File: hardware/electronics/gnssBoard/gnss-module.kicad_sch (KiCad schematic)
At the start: 41 parts, among them Q1 BSS138PS,115, Q2 BSS138PS,115, Q3 VAL, U2 ZED-F9P, U3 OPA344

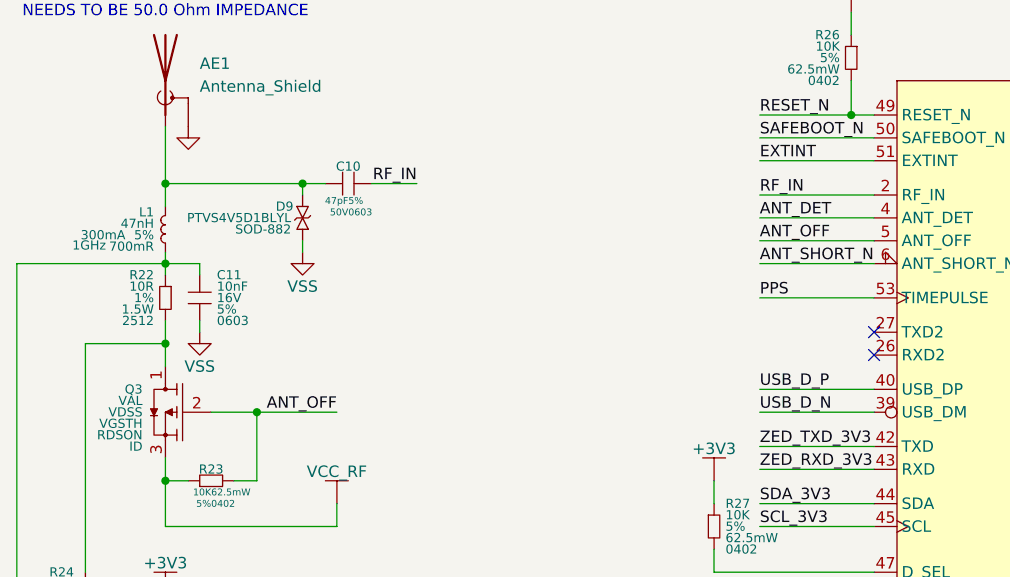
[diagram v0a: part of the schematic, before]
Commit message: applied netclasses
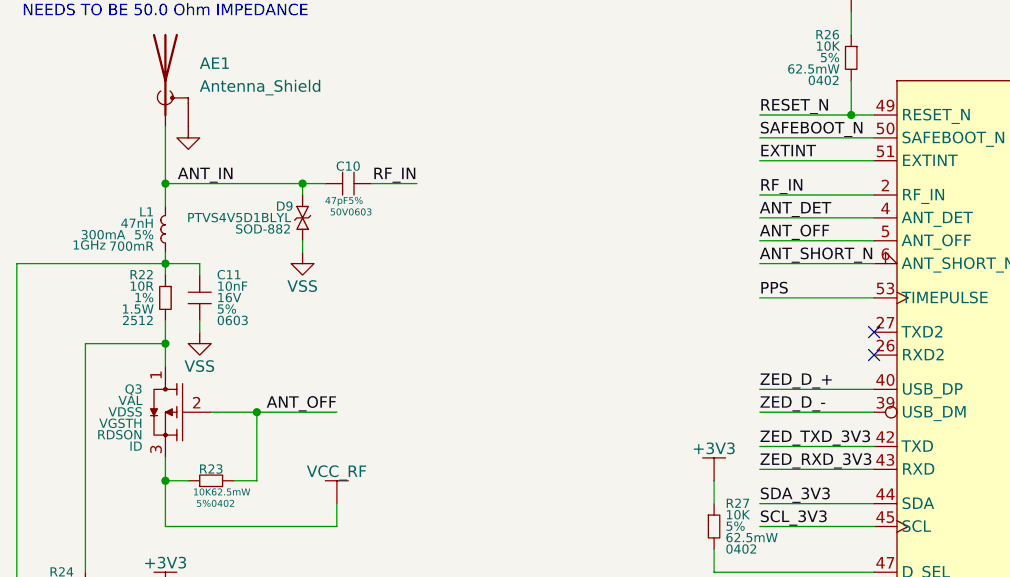
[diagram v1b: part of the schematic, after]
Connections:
- net ANT_IN: now reaches AE1.1 (A), C10.1, D9.2, L1.1
- net USB_D_N renamed ZED_D_-
- net USB_D_P renamed ZED_D_+
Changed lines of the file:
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@@
 		)
 	)
-	(label "USB_D_P"
+	(label "ZED_D_+"
 		(at 114.3 106.68 0)
 		(fields_autoplaced yes)
@@
 		)
 	)
-	(label "USB_D_N"
+	(label "ZED_D_-"
 		(at 114.3 109.22 0)
 		(fields_autoplaced yes)
@@
 		)
 	)
+	(label "ANT_IN"
+		(at 55.88 83.82 180)
+		(fields_autoplaced yes)
+		(effects
+			(font
+				(size 1.27 1.27)
+			)
+			(justify right bottom)
+		)
+	)

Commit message: work on schematic
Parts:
- AE1: value Antenna_Shield -> CONMHF1-SMD-T; footprint (none) -> lib_fp:CONMHF1; DKPN (none) -> 343-CONMHF1-SMD-TCT-ND; MPN (none) -> CONMHF1-SMD-T; Manufacturer (none) -> TE Connectivity Linx
- BT1: footprint (none) -> lib_fp:MS621FE-FL11E; CELL CELL -> Coin, 6.8mm; DKPN (none) -> 728-1057-ND; MPN (none) -> MS621FE-FL11E; Manufacturer (none) -> Seiko Instruments
- C10, C11, C5, C6, C7, C8, C9: footprint (none) -> DS-Capacitors-SMD:MLCC0603
- D7: footprint (none) -> lib_fp:LTST-0603
- D8: footprint (none) -> lib_fp:SOD123
- D9: footprint (none) -> lib_fp:SOD882
- L1: footprint (none) -> lib_fp:L_0402
- Q1, Q2: footprint (none) -> lib_fp:SOT23-6P65_210X200x110L30X25N
- Q3: value VAL -> DMG1013TQ-7; footprint (none) -> lib_fp:SOT23-3P50_160X160X75L22X22N; DKPN (none) -> 31-DMG1013TQ-7CT-ND; MPN (none) -> DMG1013TQ-7; Manufacturer (none) -> Diodes Incorporated
- R12, R13, R14, R15, R16, R17, R18, R19, R20, R21, R23, R24, R25, R26, R27: footprint (none) -> lib_fp:CRCW0402
- R22: footprint (none) -> lib_fp:CRCW2512-HP
- TP11, TP12, TP13, TP14, TP15, TP16: footprint (none) -> lib_fp:TP_1mm; DKPN (none) -> N/A; MPN (none) -> N/A; Manufacturer (none) -> N/A; now left out of the parts list
- U2: footprint DSE-RF-Receivers:ZED-F9P-04B_UBL -> lib_fp:ZED-F9P-04B_UBL
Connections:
- net ANT_OFF: now also Q3.1; no longer Q3.2
- net ANT_SHORT_N: now also U3.4 (-); no longer U3.3 (V-)
- net VCC_RF: now also Q3.2; no longer Q3.3
- net VSS: now also U3.2 (V-); no longer U3.3 (V-)
- net at R22.2, R24.1: now also Q3.3; no longer Q3.1
- net at R24.2, R25.1: now also U3.3 (+); no longer U3.4 (+)

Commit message: worked on GNSS board
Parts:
- removed Q1, Q2: BSS138PS,115, lib_fp:SOT23-6P65_210X200x110L30X25N, symbol lib_sch:Duel-NMOS
- added C5: 100nF, lib_fp:MLCC0603, symbol lib_sch:C
- added Q1, Q2, Q3, Q4: DMN2992UFB4Q-7B, lib_fp:XDFN3P35_100X60X40L15X25N, symbol DS-Transistors:NMOS_GSD
- added R21, R22: 27R, lib_fp:CRCW0402, symbol lib_sch:R_horizontal
- AE1: symbol Device:Antenna_Shield -> lib_sch:Antenna_Shield
- BT1: symbol DS-Batteries:Battery -> lib_sch:Battery
- C10: renamed from C11; footprint DS-Capacitors-SMD:MLCC0603 -> lib_fp:MLCC0603; symbol DS-Passives:C -> lib_sch:C
- C3: renamed from C5; footprint DS-Capacitors-SMD:MLCC0603 -> lib_fp:MLCC0603; symbol DS-Passives:C -> lib_sch:C
- C4: renamed from C6; footprint DS-Capacitors-SMD:MLCC0603 -> lib_fp:MLCC0603; symbol DS-Passives:C -> lib_sch:C
- C6: renamed from C7; footprint DS-Capacitors-SMD:MLCC0603 -> lib_fp:MLCC0603; symbol DS-Passives:C -> lib_sch:C
- C7: renamed from C8; footprint DS-Capacitors-SMD:MLCC0603 -> lib_fp:MLCC0603; symbol DS-Passives:C -> lib_sch:C
- C8: renamed from C9; footprint DS-Capacitors-SMD:MLCC0603 -> lib_fp:MLCC0603; symbol DS-Passives:C -> lib_sch:C
- C9: renamed from C10; footprint DS-Capacitors-SMD:MLCC0603 -> lib_fp:MLCC0603; symbol DS-Passives:C_horizontal -> lib_sch:C_horizontal
- D4: renamed from D7; symbol DS-LEDs:LED -> lib_sch:LED
- D5: renamed from D8; symbol DS-Passives:D_Schottky -> lib_sch:D_Schottky
- D6: renamed from D9; symbol DS-Passives:D_TVS -> lib_sch:D_TVS
- JP4: footprint (none) -> lib_fp:Jumper_2_Bridged; symbol DS-Jumpers:Jumper_2_Bridged -> lib_sch:Jumper_2_Bridged
- L1: symbol DS-Passives:L -> lib_sch:L
- Q5: renamed from Q3; symbol DS-Transistors:PMOS_DGS -> lib_sch:PMOS_DGS
- R10: renamed from R16; symbol DS-Passives:R -> lib_sch:R
- R11: renamed from R17; symbol DS-Passives:R -> lib_sch:R
- R12: renamed from R18; symbol DS-Passives:R -> lib_sch:R
- R13: renamed from R19; symbol DS-Passives:R -> lib_sch:R
- R14: renamed from R20; symbol DS-Passives:R -> lib_sch:R
- R15: renamed from R21; symbol DS-Passives:R -> lib_sch:R
- R16: renamed from R22; footprint lib_fp:CRCW2512-HP -> lib_fp:CRCW0603; symbol DS-Passives:R -> lib_sch:R; DKPN 541-10.0RCT-ND -> 541-10.0HCT-ND; MPN CRCW251210R0FKEGHP -> CRCW060310R0FKEA; Package 2512 -> 0603; Power Rating 1.5W -> 100mW
- R17: renamed from R23; symbol DS-Passives:R_horizontal -> lib_sch:R_horizontal
- R18: renamed from R24; symbol DS-Passives:R -> lib_sch:R
- R19: renamed from R25; symbol DS-Passives:R -> lib_sch:R
- R20: renamed from R26; symbol DS-Passives:R -> lib_sch:R
- R23: renamed from R27; symbol DS-Passives:R -> lib_sch:R
- R6: renamed from R12; symbol DS-Passives:R -> lib_sch:R
- R7: renamed from R13; symbol DS-Passives:R -> lib_sch:R
- R8: renamed from R14; symbol DS-Passives:R -> lib_sch:R
- R9: renamed from R15; symbol DS-Passives:R -> lib_sch:R
- TP11, TP12, TP13, TP14, TP15, TP16: symbol DS-Testpoints:Testpoint -> lib_sch:Testpoint
- U2: symbol DS-RF-Receivers:ZED-F9P-04B -> lib_sch:ZED-F9P-04B
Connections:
- net VBUS is gone; now on net +3V3: C6.1, C7.1, U2.38 (V_USB)
- net +1V8: now also Q1.1, Q2.1, Q3.1, Q4.1
- net +3V3: now also C5.1
- net PPS: now also R14.1; no longer D4.1
- net SCL_3V3: now also Q1.3
- net SDA_1V8: now also Q2.2; no longer R8.2
- net SDA_3V3: now also Q2.3
- net VSS: now also C5.2
- net ZED_RXD_1V8: now also Q3.2; no longer R13.2
- net ZED_RXD_3V3: now also Q3.3
- net ZED_TXD_3V3: now also Q4.3
- net at D4.2: now also JP4.2; no longer R14.1
- net at R14.2: now also D4.1; no longer JP4.2
- net ZED_D_+ renamed ZED_D+
- net ZED_D+: now also R21.2
- net ZED_D_- renamed ZED_D-
- net ZED_D-: now also R22.2
- new net HOST_D+: R21.1
- new net HOST_D-: R22.1
- new net SCL_1V8: Q1.2, R8.2
- new net ZED_TXD_1V8: Q4.2, R13.2
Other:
- moved on the sheet: C3, C4, D4, JP4, R14, R23

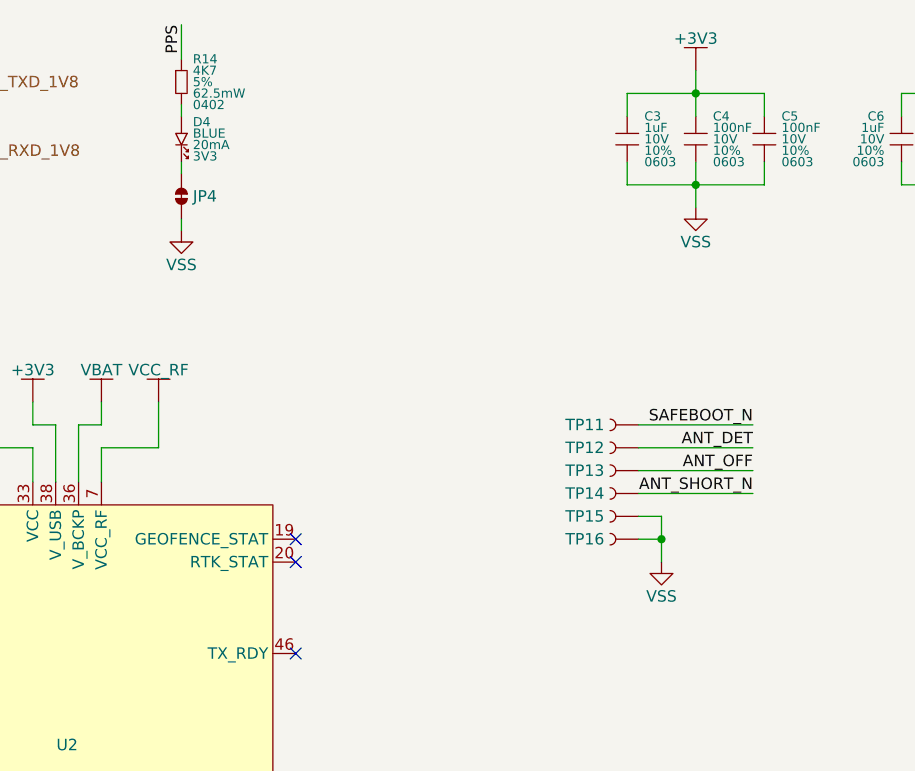
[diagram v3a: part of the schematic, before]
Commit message: Got rid of test points due to space constraints
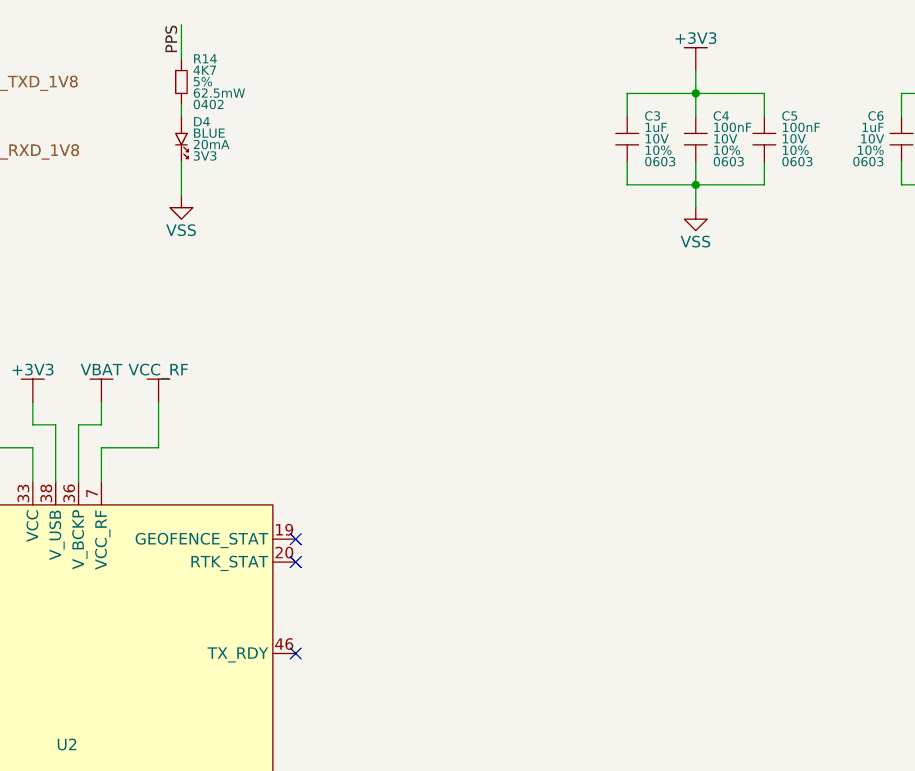
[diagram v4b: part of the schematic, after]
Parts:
- removed JP4: ~, lib_fp:Jumper_2_Bridged, symbol lib_sch:Jumper_2_Bridged
- removed TP11, TP12, TP13, TP14, TP15, TP16: ~, lib_fp:TP_1mm, symbol lib_sch:Testpoint
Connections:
- net VSS: now also D4.2

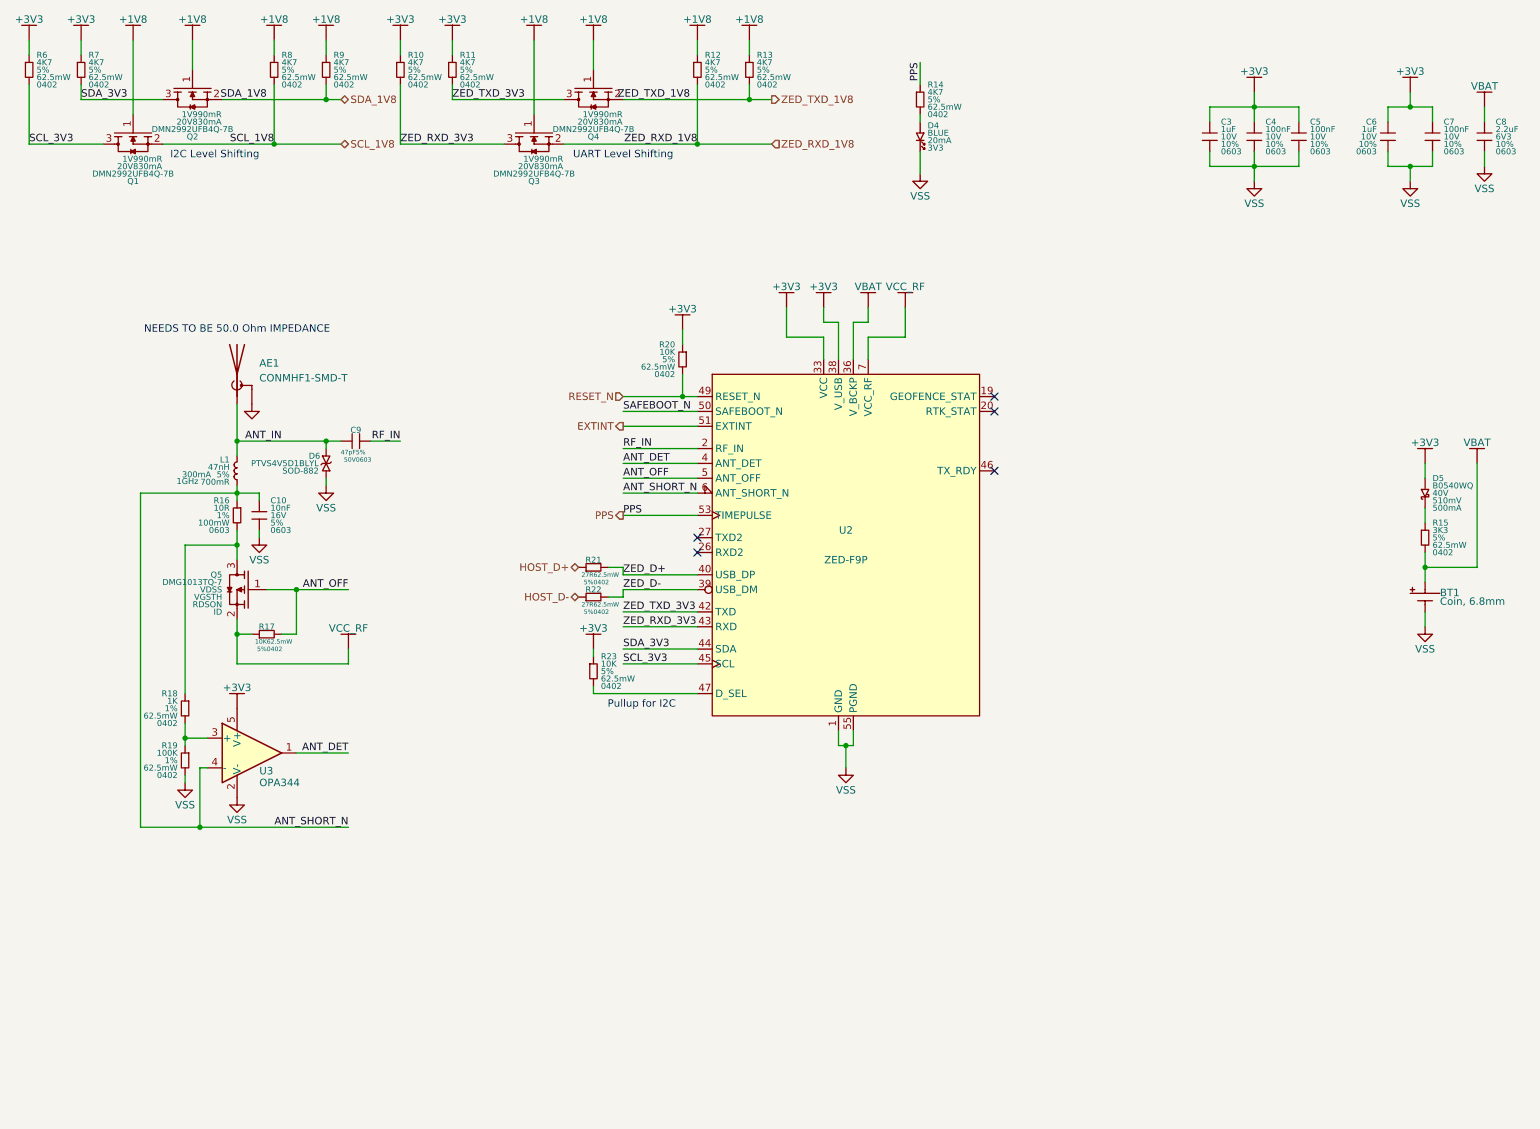
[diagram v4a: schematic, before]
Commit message: replaced MOSFETS with TI multi-channel level shifter
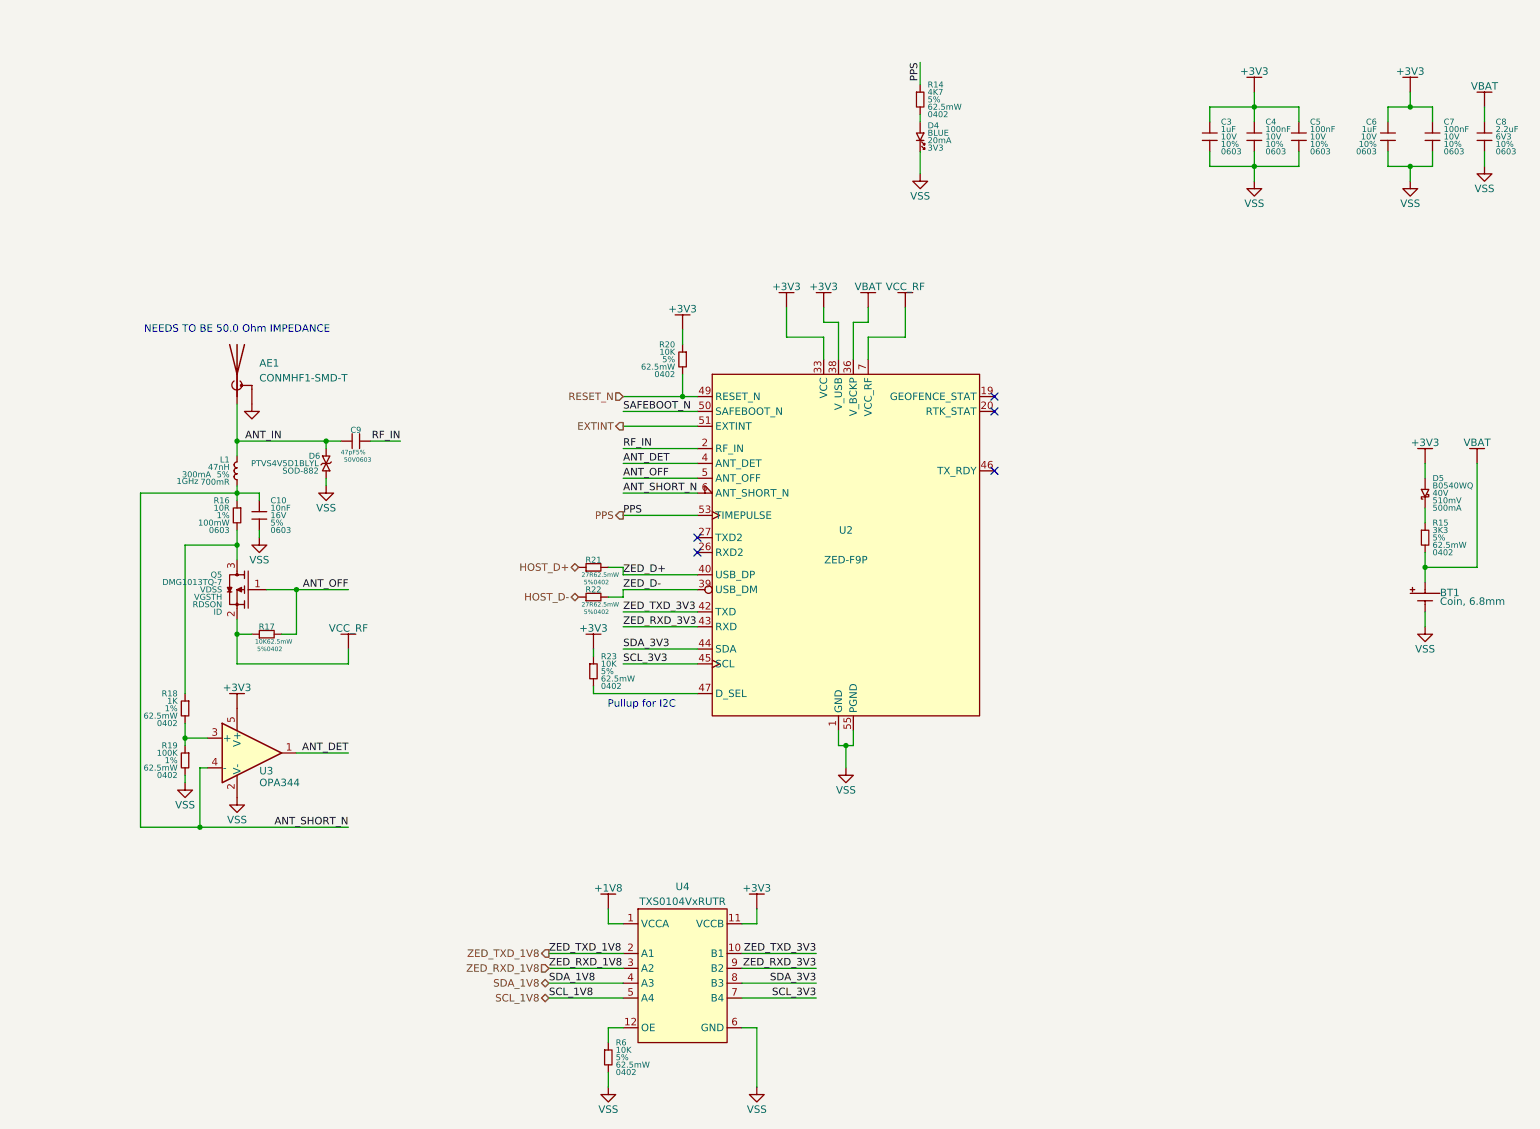
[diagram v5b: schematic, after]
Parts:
- removed Q1, Q2, Q3, Q4: DMN2992UFB4Q-7B, lib_fp:XDFN3P35_100X60X40L15X25N, symbol DS-Transistors:NMOS_GSD
- removed R10, R11, R12, R13, R7, R8, R9: 4K7, lib_fp:CRCW0402, symbol lib_sch:R
- added U4: TXS0104VxRUTR, lib_fp:RUT0012A, symbol lib_sch:TXS0104VxRUTR
- R6: value 4K7 -> 10K; DKPN 541-4.7KJCT-ND -> 541-10KJCT-ND; MPN CRCW04024K70JNED -> CRCW040210K0JNED
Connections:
- net +1V8: now also U4.1 (VCCA)
- net +3V3: now also U4.11 (VCCB); no longer R6.1
- net SCL_1V8: now also U4.5 (A4)
- net SCL_3V3: now also U4.7 (B4); no longer R6.2
- net SDA_1V8: now also U4.4 (A3)
- net SDA_3V3: now also U4.8 (B3)
- net VSS: now also R6.2, U4.6 (GND)
- net ZED_RXD_1V8: now also U4.3 (A2)
- net ZED_RXD_3V3: now also U4.9 (B2)
- net ZED_TXD_1V8: now also U4.2 (A1)
- net ZED_TXD_3V3: now also U4.10 (B1)
- new net: R6.1, U4.12 (OE)
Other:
- note removed: "I2C Level Shifting"
- note removed: "UART Level Shifting"
